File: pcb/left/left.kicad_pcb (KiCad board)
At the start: 2 copper layers, 149.9 x 116.8 mm, 66 parts, among them J1 RJ45-8pin, K1 Key00, K10 Key12, K11 Key22, K12 Key32, K13 Key03, K14 Key13, K15 Key23, K16 Key33, K17 Key04, K18 Key14, K19 Key24, K2 Key10, K20 Key34, K21 Key05, K22 Key15, K23 Key25, K24 Key35, K3 Key20, K4 Key30, K40 Key_thumb, K5 Key01, K6 Key11, K7 Key21, K8 Key31, K9 Key02, U1 Arduino_Pro_Micro, U2 JT8P-3.2T-B10K-1-16Y

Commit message: improve pcb design
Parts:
- added D3: D, Diodes_THT:D_DO-35_SOD27_P7.62mm_Horizontal, F.Cu at (127.2, 85.1)
- added D31: D, Diodes_THT:D_DO-35_SOD27_P7.62mm_Horizontal, F.Cu at (129.5, 96.5)
- added K41: Mouse_Mode, Buttons_Switches_THT:SW_Tactile_SPST_Angled_PTS645Vx31-2LFS, F.Cu at (129.5, 101.6)
- added REF**: MountingHole_3.2mm_M3, Mounting_Holes:MountingHole_3.2mm_M3, F.Cu at (17.1, 19.7)
- added REF**: MountingHole_3.2mm_M3, Mounting_Holes:MountingHole_3.2mm_M3, F.Cu at (17.1, 57.8)
- added REF**: MountingHole_3.2mm_M3, Mounting_Holes:MountingHole_3.2mm_M3, F.Cu at (93.3, 14.6)
- added REF**: MountingHole_3.2mm_M3, Mounting_Holes:MountingHole_3.2mm_M3, F.Cu at (104.1, 88.9)
- K40: footprint 4x6t2:SW_Cherry_MX1A_1.00u_r30_Plate -> Buttons_Switches_Keyboard:SW_Cherry_MX1A_1.50u_Plate
- U2: footprint 4x6t2:JT8P-3.2T-B10K-1-16Y -> 4x6t2:JT8P-3.2T-B10K-1-16Y_DIP
- moved U2 82.2 mm to (123.2, 43.2), turned to 90 degrees
- moved LEDR3 58.0 mm to (134.6, 34.3), turned to 180 degrees
- moved D29 53.9 mm to (137.2, 34.3), turned to 90 degrees
- moved LEDR2 52.3 mm to (134.6, 39.4), turned to 180 degrees
- moved D2 48.3 mm to (137.2, 39.4), turned to 90 degrees
- moved LEDR1 47.0 mm to (134.6, 44.5), turned to 180 degrees
- moved D1 43.3 mm to (137.2, 44.5), turned to 90 degrees
- moved REF** 32.0 mm to (135.9, 26.7)
- moved U1 30.7 mm to (123.2, 14.0)
- moved REF** 30.7 mm to (116.8, -3.81)
- moved REF** 30.7 mm to (129.5, -3.81)
- moved PassC1 30.7 mm to (129.5, 7.62)
- moved D11 25.4 mm to (92.7, 59.7)
- moved D15 25.4 mm to (73.7, 54.6)
- moved D10 25.4 mm to (92.7, 40.6)
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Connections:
- K40 pad 1: /Thumb -> /ROW3
- K40 pad 2: GND -> Net-(D3-Pad1)
- U1 pad 13: /Thumb -> /COL6
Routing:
- net /ROW2: track 0.00 -> 224.5 mm, vias 0 -> 2
- net /ROW3: track 0.00 -> 210.3 mm, vias 0 -> 2
- net /COL5: track 0.00 -> 162.8 mm
- net GND: track 0.00 -> 145.9 mm, vias 0 -> 1
- net /COL4: track 0.00 -> 139.9 mm, vias 0 -> 1
- net /ROW1: track 0.00 -> 134.0 mm, vias 0 -> 2
- net /ROW0: track 0.00 -> 132.4 mm
- net /COL3: track 0.00 -> 121.5 mm
- net /COL2: track 0.00 -> 101.8 mm, vias 0 -> 1
- net /COL1: track 0.00 -> 86.2 mm
- net /RST: track 0.00 -> 83.1 mm, vias 0 -> 1
- net /SCL: track 0.00 -> 82.3 mm, vias 0 -> 3
- net +5V: track 0.00 -> 81.8 mm, vias 0 -> 2
- net /COL6: track 0.00 -> 79.5 mm, vias 0 -> 1
- net /SDA: track 0.00 -> 77.2 mm, vias 0 -> 3
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- added copper zone on B.Cu, net GND
- added copper zone on F.Cu, net GND
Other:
- board size 149.9 x 116.8 mm -> 141 x 116.8 mm
- net class Default: clearance 0.2 -> 0.203
- rule trace_clearance: 0.2 -> 0.203
- rule trace_min: 0.2 -> 0.203

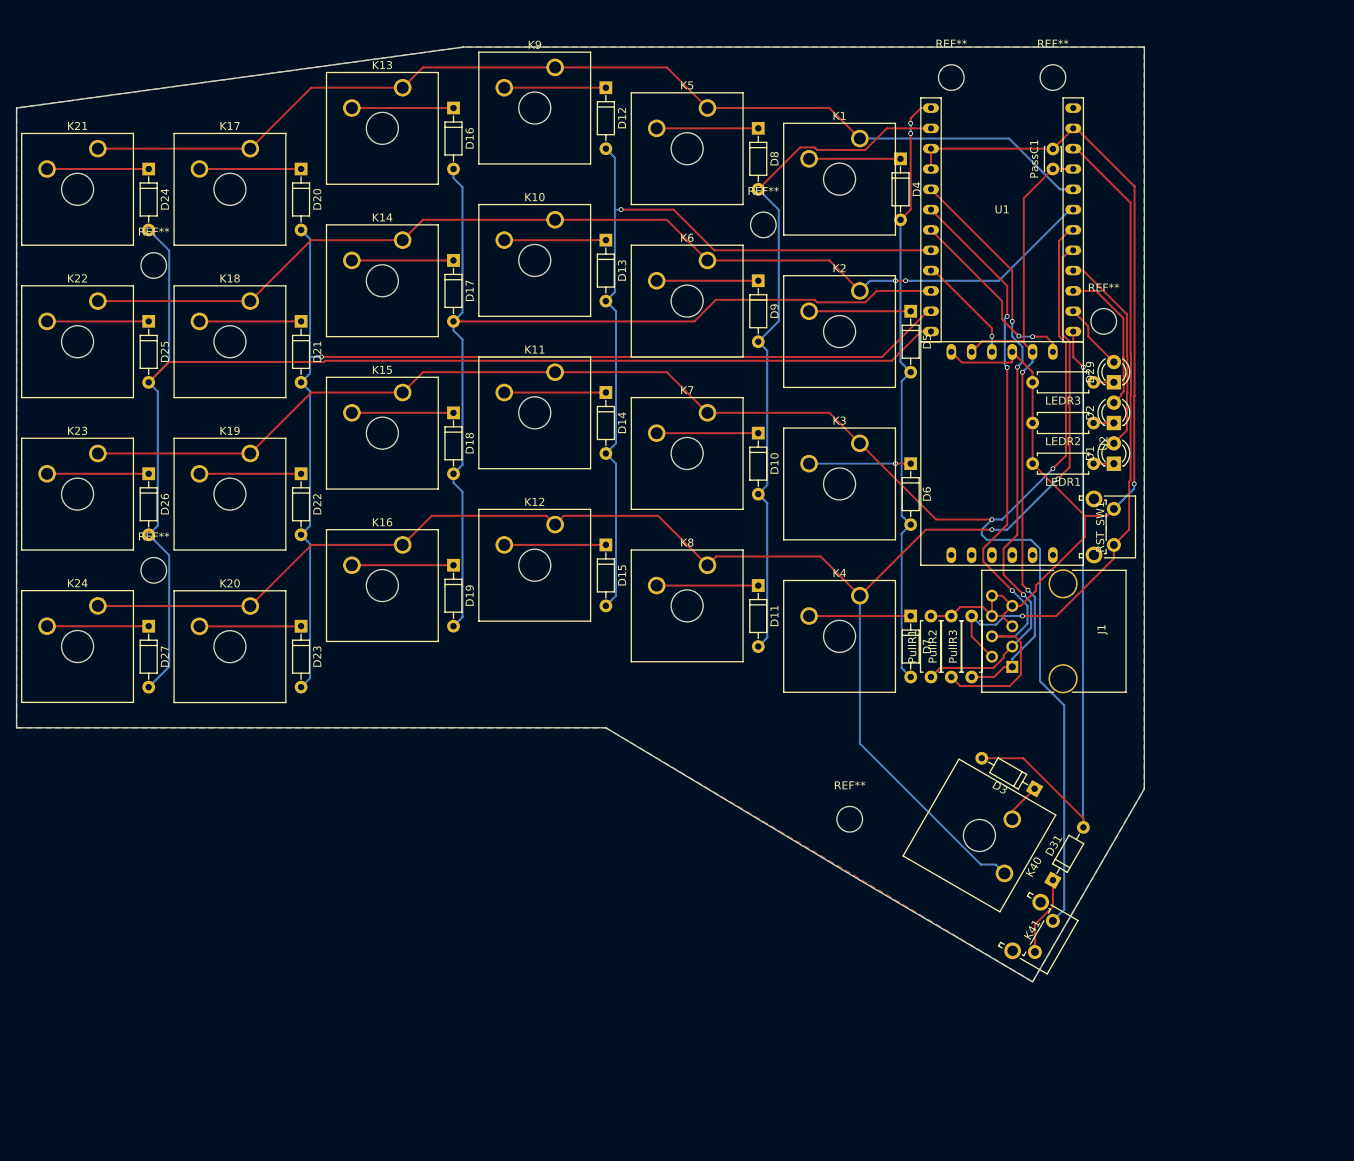
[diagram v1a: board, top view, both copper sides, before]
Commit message: improve key arrangement
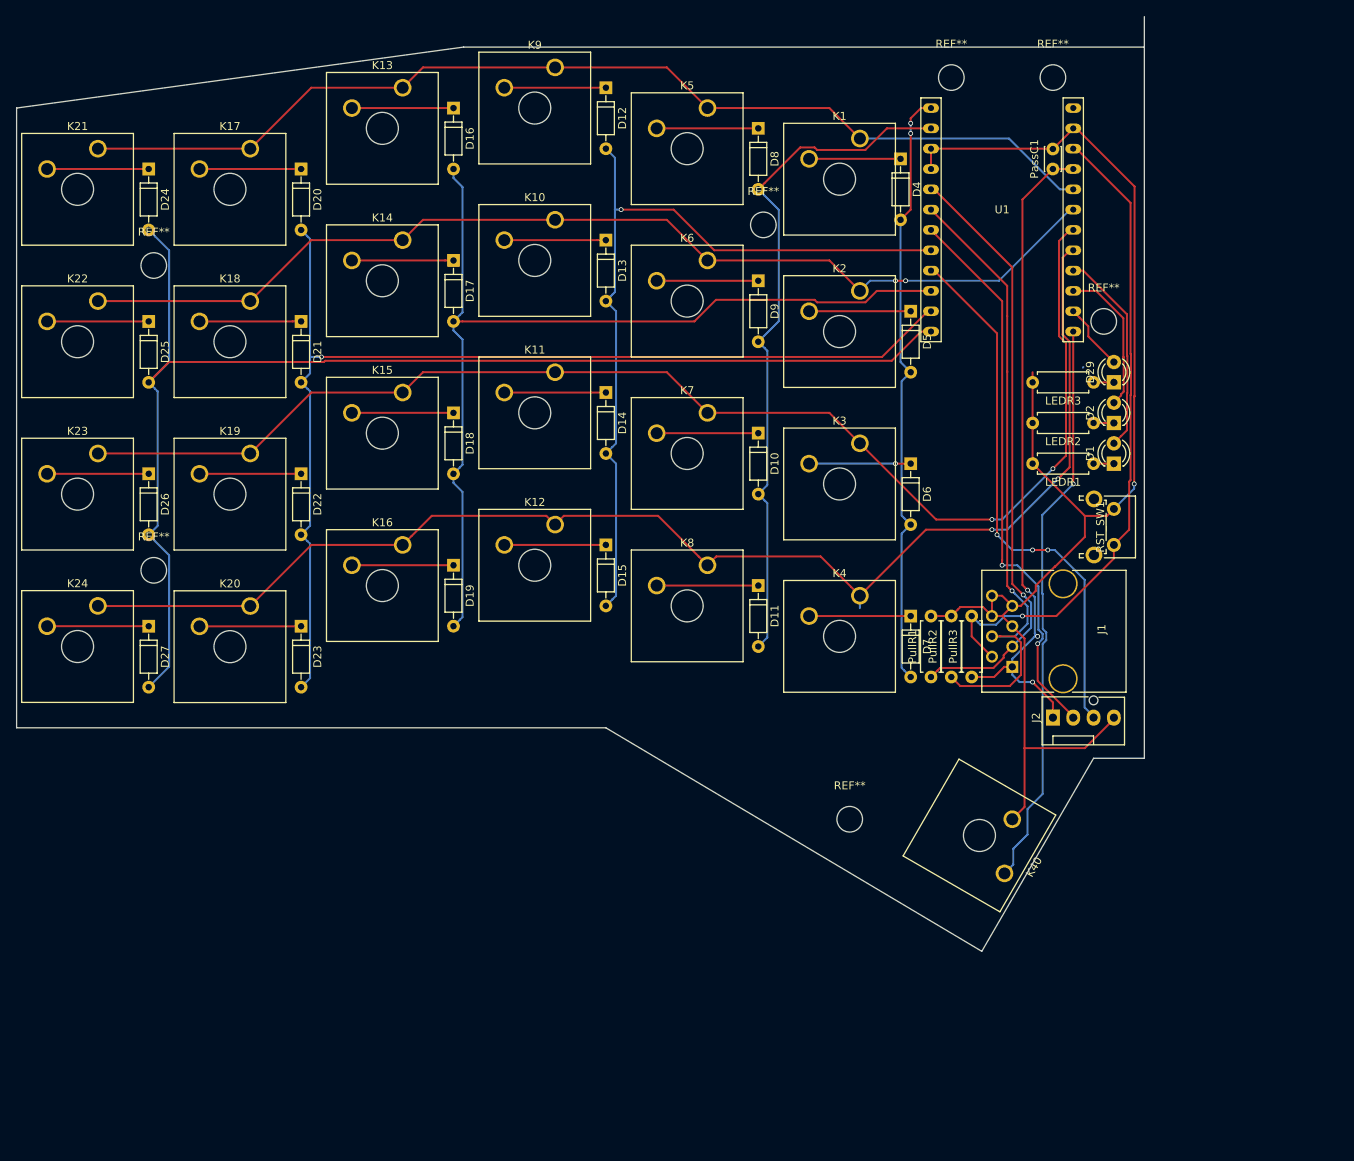
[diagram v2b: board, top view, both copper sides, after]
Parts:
- removed D3, D31: D, Diodes_THT:D_DO-35_SOD27_P7.62mm_Horizontal
- removed K41: Mouse_Mode, Buttons_Switches_THT:SW_Tactile_SPST_Angled_PTS645Vx31-2LFS
- removed U2: JT8P-3.2T-B10K-1-16Y, 4x6t2:JT8P-3.2T-B10K-1-16Y_DIP
- added J2: Conn_01x04, Connectors:Fan_Pin_Header_Straight_1x04, F.Cu at (129.5, 76.2)
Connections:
- K40 pad 1: /ROW3 -> /Thumb_key
- K40 pad 2: Net-(D3-Pad1) -> GND
- U1 pad 13: /COL6 -> /Thumb_key
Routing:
- net /COL6: track 79.5 -> 0.00 mm, vias 1 -> 0
- net /Thumb_key: track 0.00 -> 71.7 mm, vias 0 -> 1
- net /ROW2: track 224.5 -> 165.7 mm
- net /Y: track 13.6 -> 67.6 mm, vias 1 -> 3
- net /X: track 23.5 -> 70.0 mm
- net /ROW3: track 210.3 -> 168.6 mm
- net GND: track 145.9 -> 171.1 mm
- net Net-(D31-Pad1): track 9.91 -> 0.00 mm
- net Net-(D3-Pad1): track 4.97 -> 0.00 mm
- net /SCL: track 82.3 -> 79.8 mm, vias 3 -> 1
- net +5V: track 81.8 -> 83.8 mm, vias 2 -> 3
- net /SDA: track 77.2 -> 75.5 mm, vias 3 -> 1
- removed copper zone on B.Cu, net GND
- removed copper zone on F.Cu, net GND
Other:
- outline, holes or cut-outs redrawn
